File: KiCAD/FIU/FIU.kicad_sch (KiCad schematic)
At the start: 17 parts, among them U1 STM32F303RETx, Y1 12Mhz

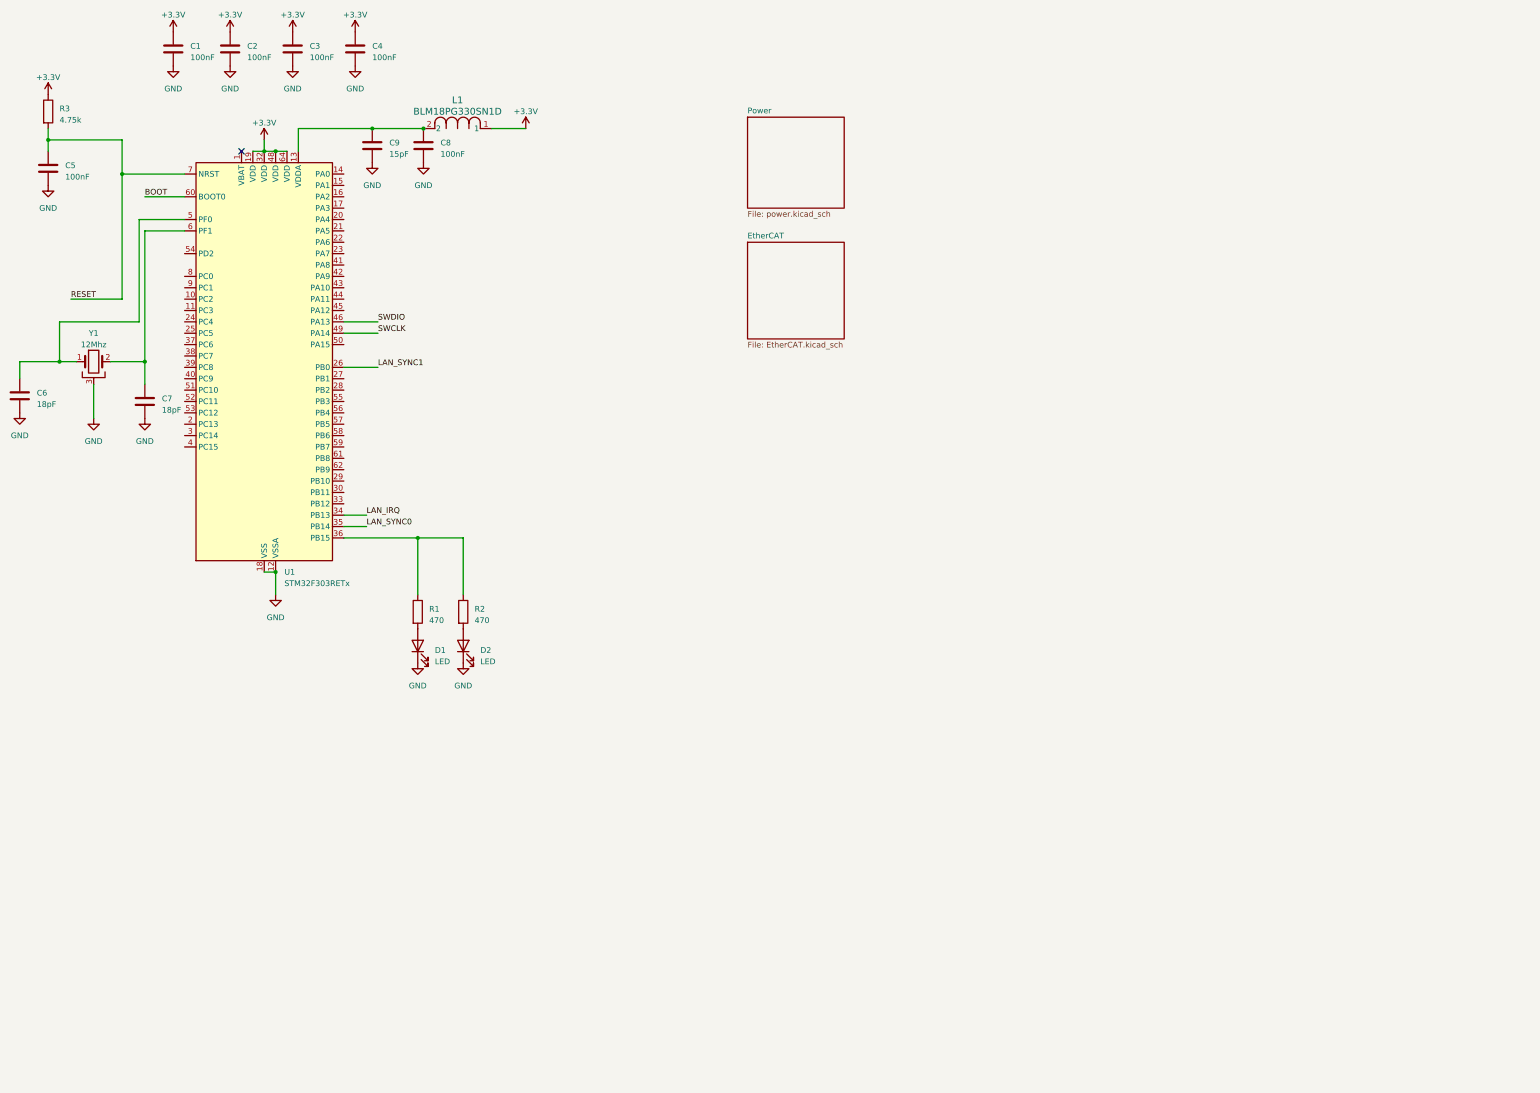
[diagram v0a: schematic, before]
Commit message: finished ethercat part
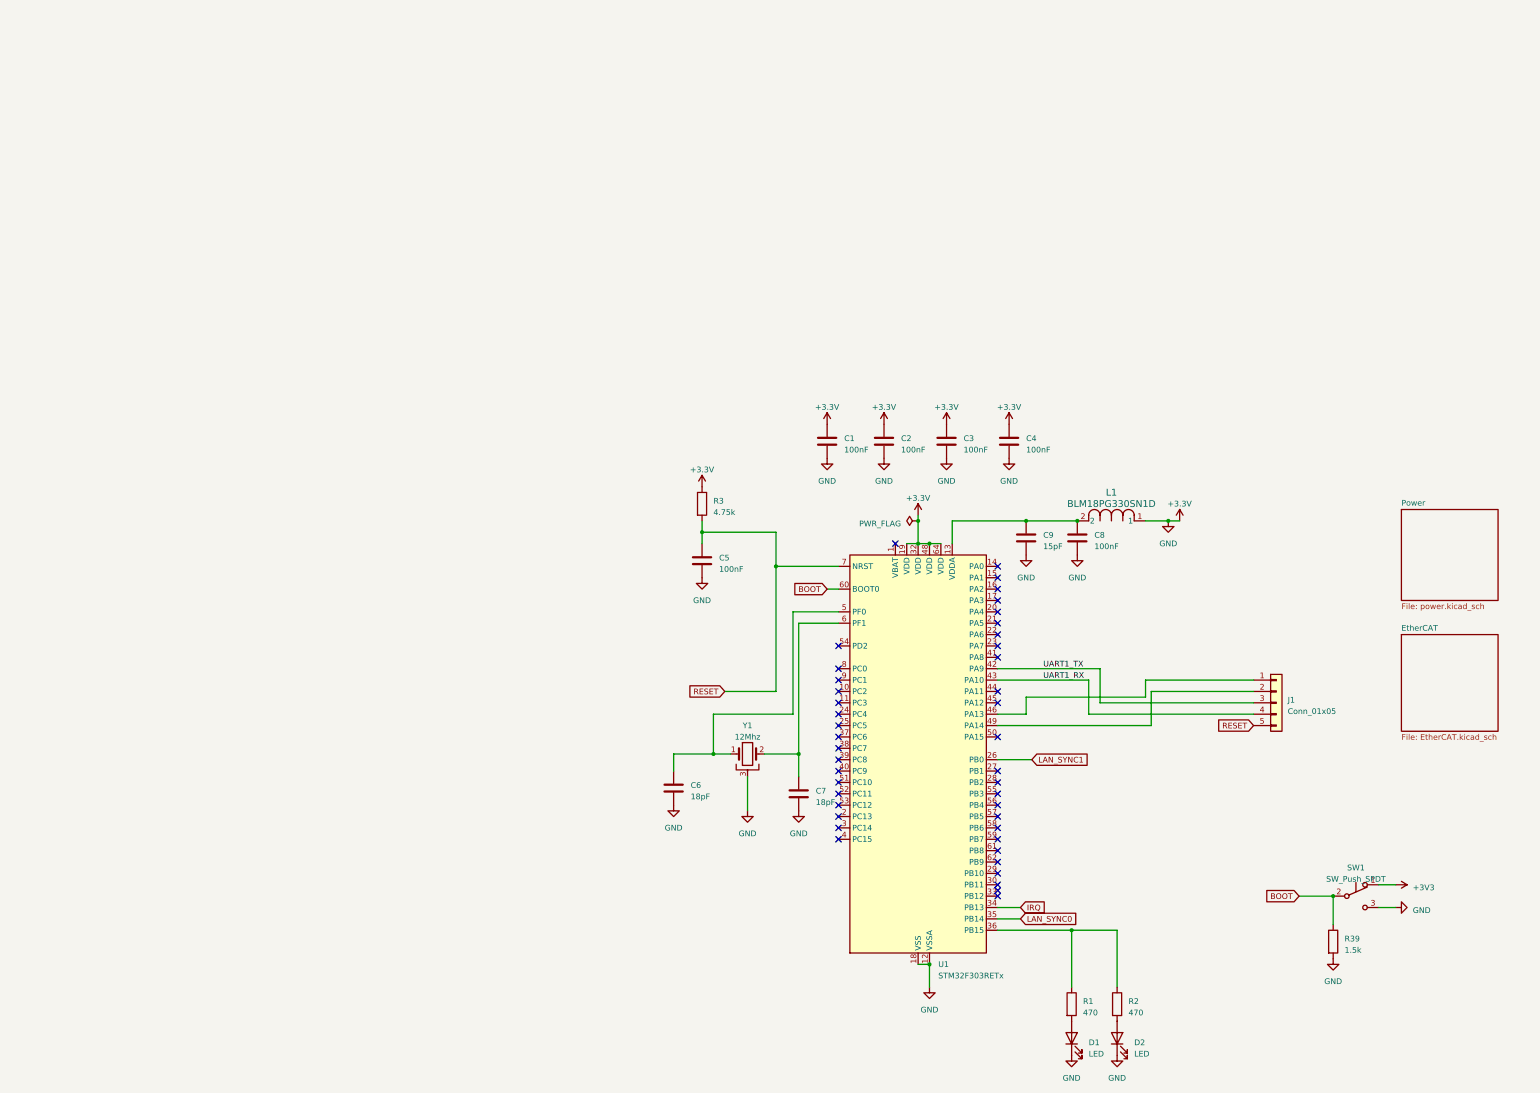
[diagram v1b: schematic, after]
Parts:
- added J1: Conn_01x05, symbol Connector_Generic:Conn_01x05
- added R39: 1.5k, symbol Device:R
- added SW1: SW_Push_SPDT, symbol Switch:SW_Push_SPDT
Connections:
- net GND is gone; now on net +3.3V: C1.2, C2.2, C3.2, C4.2, C5.2, C6.2, C7.2, C8.2, C9.2, D1.1 (K), D2.1 (K), U1.12 (VSSA), U1.18 (VSS), U1.31 (VSS), U1.47 (VSS), U1.63 (VSS), Y1.3
- net +3.3V: now also R39.2, SW1.3 (C)
- net BOOT: now also R39.1, SW1.2 (B)
- net RESET: now also J1.5 (Pin_5)
- net UART1_TX: now reaches U1.42 (PA9)
- net UART1_TX: now also J1.3 (Pin_3)
- net UART1_RX: now reaches U1.43 (PA10)
- net UART1_RX: now also J1.4 (Pin_4)
- net LAN_IRQ renamed IRQ
- net SWCLK: no longer names the net of U1.49 (PA14)
- net SWCLK: now also J1.2 (Pin_2)
- net SWDIO: no longer names the net of U1.46 (PA13)
- net SWDIO: now also J1.1 (Pin_1)
- new net +3V3: SW1.1 (A)
- no-connect marks 1 -> 43
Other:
- moved on the sheet: C1, C2, C3, C4, C5, C6, C7, C8, C9, D1, D2, L1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

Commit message: new level
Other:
- added sheet fiu_board (fiu_board.kicad_sch)
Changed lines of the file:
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@@
+    )
+  )
+  (sheet (at 119.38 97.79) (size 29.21 30.48) (fields_autoplaced)
+    (stroke (width 0.1524) (type solid))
+    (fill (color 0 0 0 0.0000))
+    (property "Sheetname" "fiu_board" (at 119.38 97.0784 0)
+      (effects (font (size 1.27 1.27)) (justify left bottom))
+    )
+    (property "Sheetfile" "fiu_board.kicad_sch" (at 119.38 128.8546 0)
+      (effects (font (size 1.27 1.27)) (justify left top))
+    )
+    (instances
+      (project "FIU"
+        (path "/be6e6856-a046-4a03-bd27-192402d12712" (page "4"))
+      )
     )
   )

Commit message: updated libraries
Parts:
- removed C1, C2, C3, C4, C5, C8: 100nF, Capacitor_SMD:C_0805_2012Metric_Pad1.18x1.45mm_HandSolder, symbol Device:C
- removed C6, C7: 18pF, Capacitor_SMD:C_0805_2012Metric_Pad1.18x1.45mm_HandSolder, symbol Device:C
- removed C9: 15pF, Capacitor_SMD:C_0805_2012Metric_Pad1.18x1.45mm_HandSolder, symbol Device:C
- added C24 (x6): 0.1uF, GRM155R71H104KE14J:CAP_GRM155R71H104KE14J_MUR, symbol GRM155R71H104KE14J:GRM155R71H104KE14J
- added C62: 15pF, Murata 15pF:G-033_MUR, symbol Murata 15pF:GRM0335C1H150JA01D
- added C62 (x2): 18pF, Murata 15pF:G-033_MUR, symbol Murata 18pF:GRM0335C1H180JA01D
- D1: footprint (none) -> LED_SMD:LED_1206_3216Metric_Pad1.42x1.75mm_HandSolder
- D2: footprint (none) -> LED_SMD:LED_0805_2012Metric_Pad1.15x1.40mm_HandSolder
- L1: footprint IND_BLM18_0603_MUR -> IND_BLM18_0603_MUR':IND_BLM18_0603_MUR
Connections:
- net +3.3V: now also C24.2, C24.2, C24.2, C24.2; no longer D1.1 (K), D2.1 (K), R39.2, SW1.3 (C), U1.12 (VSSA), U1.18 (VSS), U1.31 (VSS), U1.47 (VSS), U1.63 (VSS), Y1.3
- net RESET: now also C24.2
- net at L1.2, U1.13 (VDDA): now also C24.2, C62.2
- net at U1.5 (PF0), Y1.1: now also C62.2
- net at U1.6 (PF1), Y1.2: now also C62.2
- new net GND: C24.1, C24.1, C24.1, C24.1, C24.1, C24.1, C62.1, C62.1, C62.1, D1.1 (K), D2.1 (K), R39.2, SW1.3 (C), U1.12 (VSSA), U1.18 (VSS), U1.31 (VSS), U1.47 (VSS), U1.63 (VSS), Y1.3
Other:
- removed sheet fiu_board

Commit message: finished front of pcb
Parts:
- removed R1, R2: 470, symbol Device:R
- removed R3: 4.75k, symbol Device:R
- removed SW1: SW_Push_SPDT, symbol Switch:SW_Push_SPDT
- removed Y1: 12Mhz, symbol Device:Crystal_GND3
- added R1, R2: 470, Panasonic 470Ohm:RC0603N_PAN, symbol Panasonic 470Ohm:ERA-3AEB471V
- added R40: 4.75k, Panasonic 4.75kOhm:RC0402N_PAN-L, symbol Panasonic 4.75kOhm:ERJ-2RKF4751X
- added SW1: SW_Push_Open_Dual, Button_Switch_SMD:SW_SPST_Panasonic_EVQPL_3PL_5PL_PT_A15, symbol Switch:SW_Push_Open_Dual
- added Y3: 12Mhz, Abracon 12Mhz 18pF:CRYSTAL_ABM8G_ABR, symbol Abracon 12Mhz 18pF:ABM8G-12.000MHZ-18-D2Y-T
- D1: footprint LED_SMD:LED_1206_3216Metric_Pad1.42x1.75mm_HandSolder -> LED_SMD:LED_0603_1608Metric_Pad1.05x0.95mm_HandSolder
- D2: footprint LED_SMD:LED_0805_2012Metric_Pad1.15x1.40mm_HandSolder -> LED_SMD:LED_0603_1608Metric_Pad1.05x0.95mm_HandSolder
- J1: footprint (none) -> Connector_PinHeader_2.54mm:PinHeader_1x05_P2.54mm_Vertical
- R39: footprint (none) -> Resistor_SMD:R_0805_2012Metric_Pad1.20x1.40mm_HandSolder
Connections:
- net +3.3V: now also R40.1
- net +3V3: now also SW1.2
- net BOOT: now also SW1.1
- net GND: now also SW1.3, SW1.4, Y3.2, Y3.4
- net RESET: now also R40.2
- net at D1.2 (A): now also R1.2
- net at U1.36 (PB15): now also R1.1, R2.1
- net at C62.2, U1.5 (PF0): now also Y3.1
- net at C62.2, U1.6 (PF1): now also Y3.3
- net at D2.2 (A): now also R2.2
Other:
- moved on the sheet: C62, D2, R39
